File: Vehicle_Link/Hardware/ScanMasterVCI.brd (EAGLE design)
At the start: 53 x 39.4 mm, 97 parts, among them IC1 XMEGA32A4U, IC2 TL331, IC3 TL331, Q1 MMBT4403, Q10 ZXMP6A17G, Q2 MMBT3904, Q3 MMBT3904, Q4 MMBT4403, Q7 MMBT3904, Q8 MMBT4403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

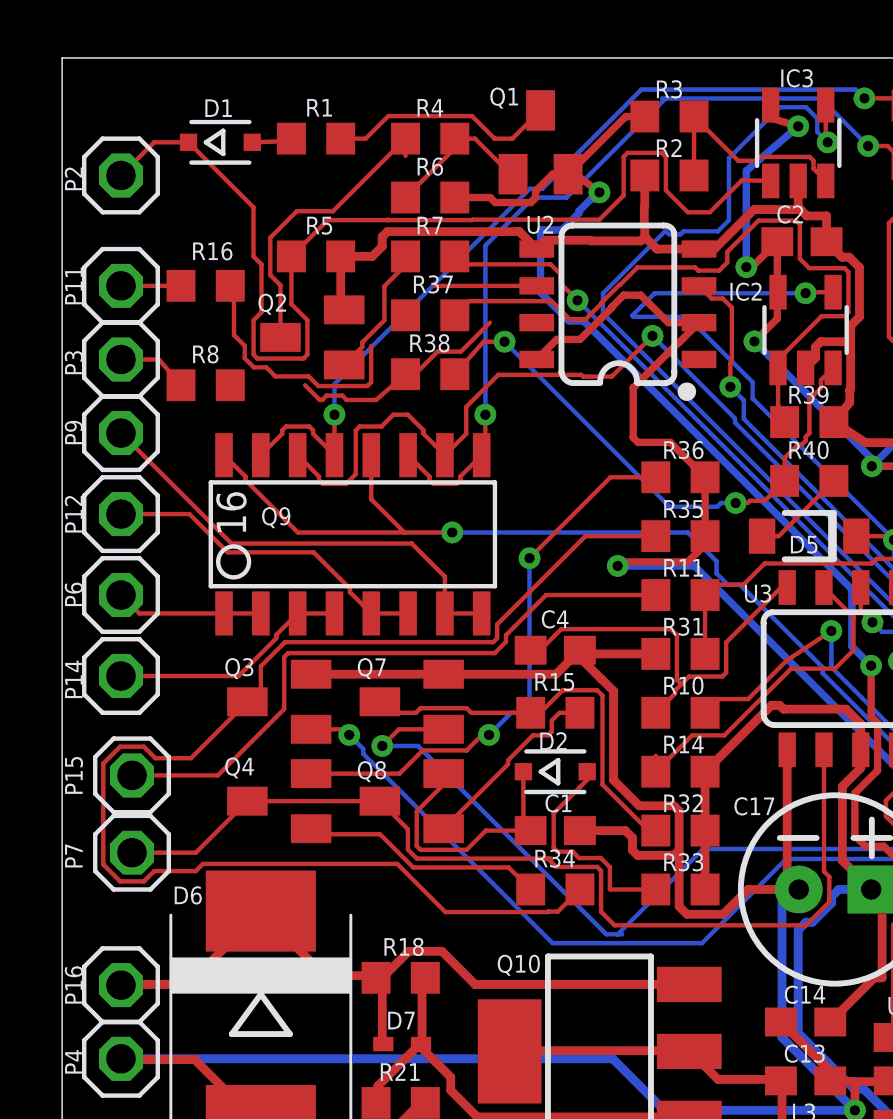
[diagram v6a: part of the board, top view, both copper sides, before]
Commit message: Some more minor changes to the schematic, some pull-up resistors needed to be moved for proper transistor-enabled pull-up resistor action. Tested on circuit, working OK now.
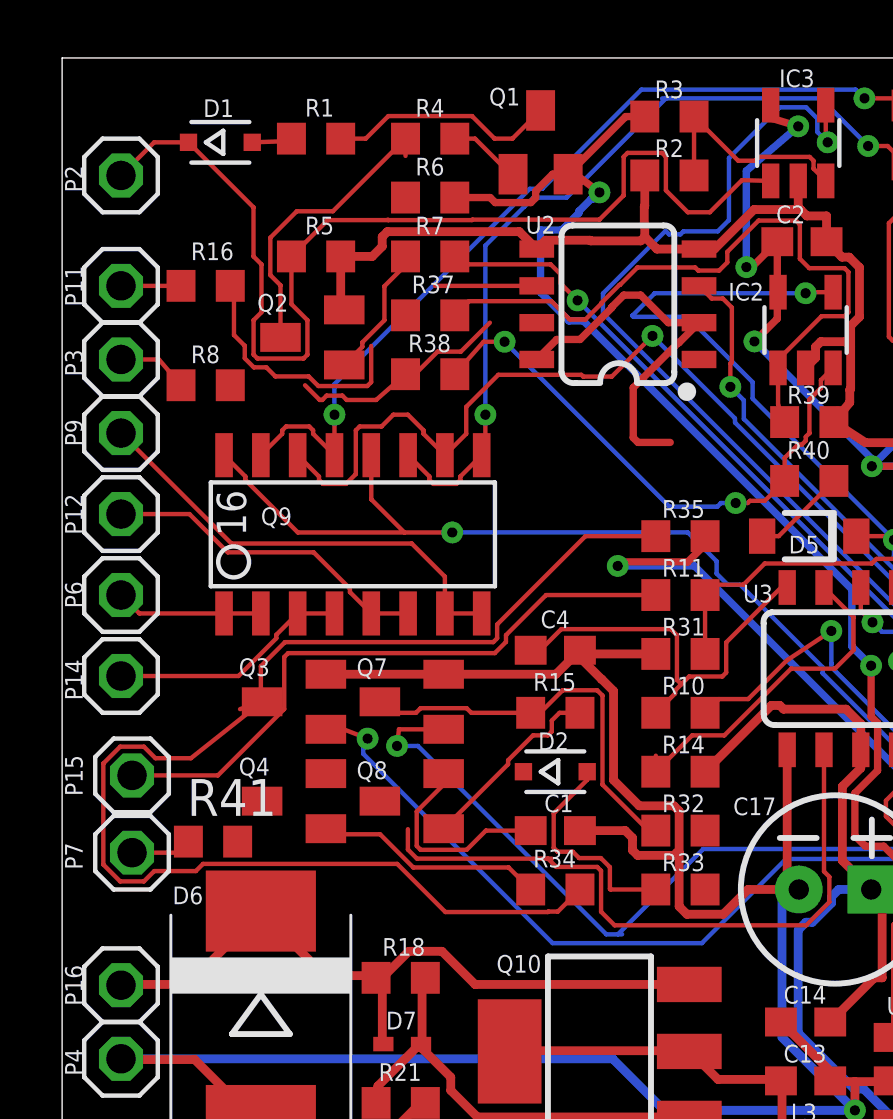
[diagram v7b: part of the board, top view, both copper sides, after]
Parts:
- removed R36: 1k, adafruit:R0603
- added R41: 1k, adafruit:R0603
- moved Q3 0.51 mm to (8.00, 17.1)
- moved Q4 0.51 mm to (8.00, 13.7)
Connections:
- removed net N$21: C1.1, D2.C, Q8.E
- new net N$32: Q8.C, R33.1
- net +12V: now also C1.1, Q8.E; no longer R33.1
- net +5V: now also Q4.E; no longer R36.2
- net J1962-7: now also D2.C, R41.1; no longer Q4.C, Q8.C
- net N$26: now also R6.1
- net N$28: no longer R6.1
- net N$31: now also Q4.C, R41.2; no longer Q4.E, R36.1
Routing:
- net N$31: track 19.3 -> 0.00 mm, vias 2 -> 0
- net N$21: track 9.33 -> 0.00 mm
- net J1962-7: track 33.7 -> 25.2 mm
- net +5V: track 82.5 -> 78.7 mm
- net +12V: track 68.4 -> 71.8 mm
- net N$28: track 5.35 -> 2.89 mm
- net N$13: track 27.4 -> 26.7 mm
- net N$23: track 45.2 -> 45.8 mm
- net GND: track 281.2 -> 280.7 mm

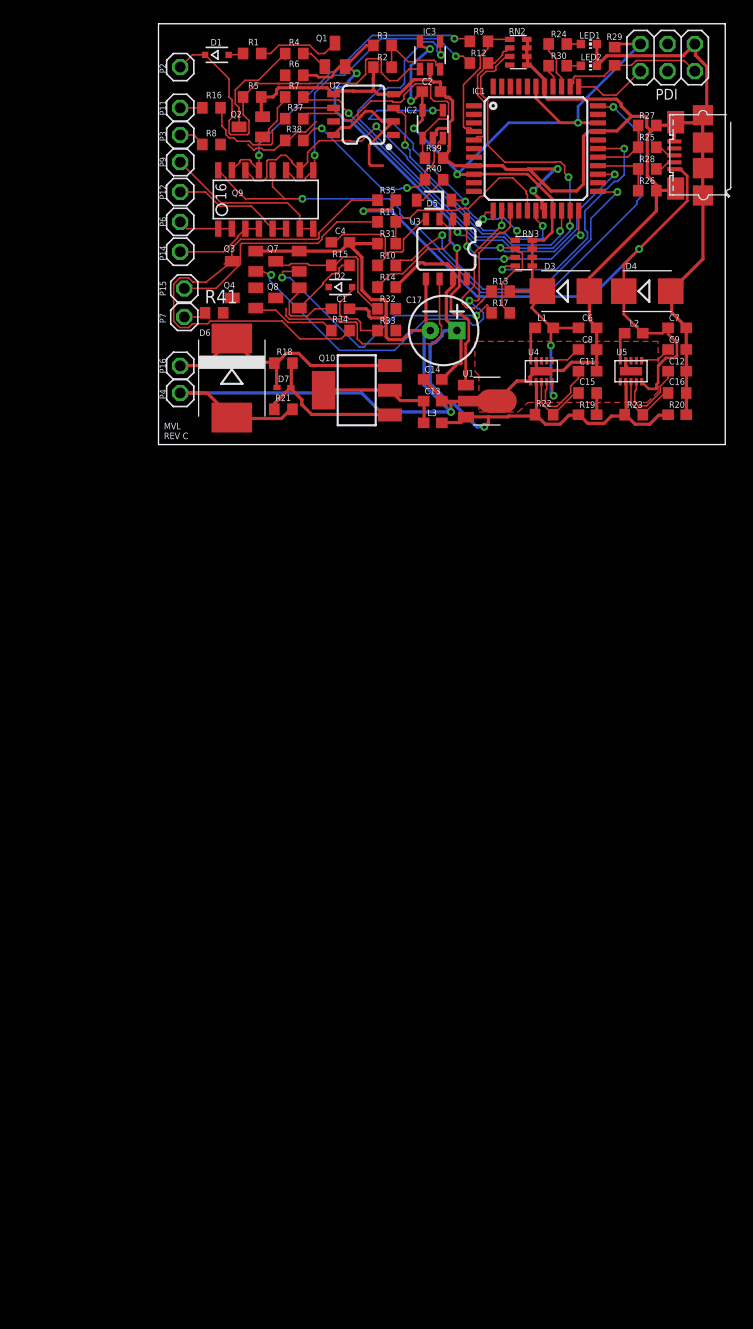
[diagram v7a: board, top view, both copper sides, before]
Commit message: Started experimenting with MOSFETs, added new parts to the library for the connector I'm planning on using.
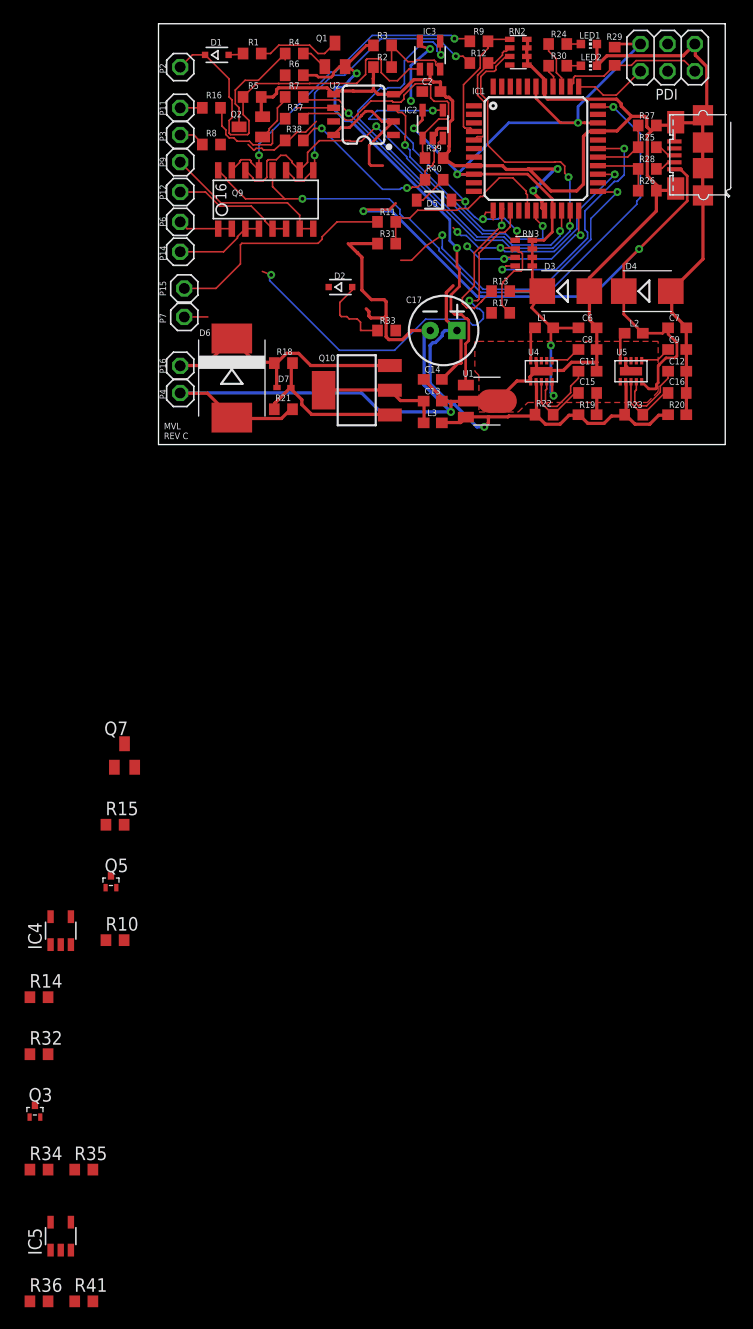
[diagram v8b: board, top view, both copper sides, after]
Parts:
- removed C1, C4: 220pF, adafruit:C0603
- removed Q4, Q8: MMBT4403, transistor-pnp:SOT23-BEC
- removed U3: SN65HVDA195-Q1, customics:SO08
- added IC4, IC5: TL331, linear:DBV-R-PDSO-G5
- added Q5: RUM002N05, customics:EMT3
- added R36: 1k, adafruit:R0603
- Q3: value MMBT3904 -> RUM002N05; device semicon-smd-ipc:SOT23 -> customics:EMT3
- R17, R34: value 1k -> 470
- R33: value 1k -> 10k
- moved R35 95.0 mm to (-6.99, -67.8)
- moved R41 93.3 mm to (-6.99, -80.1)
- moved R34 83.4 mm to (-11.2, -67.8), turned to 0 degrees
- moved Q3 81.9 mm to (-11.6, -62.4), turned to 0 degrees
- moved R32 76.9 mm to (-11.2, -57.0), turned to 0 degrees
- moved R14 74.0 mm to (-11.2, -51.7), turned to 0 degrees
- moved R10 68.0 mm to (-4.06, -46.4), turned to 0 degrees
- moved R15 56.4 mm to (-4.06, -35.6)
- moved Q7 48.7 mm to (-3.17, -29.1), turned to 0 degrees
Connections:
- removed net N$22: Q4.B, R34.2
- removed net N$23: Q3.3, R34.1, R35.1
- removed net N$31: Q4.C, R41.2
- removed net N$32: Q8.C, R33.1
- new net ISO-K: D2.C, IC4.1, Q5.2, Q7.3
- new net SCI-A-RX: IC5.1, Q3.2
- net +12V: now also IC4.5, IC5.5, R14.2, R33.1; no longer C1.1, Q8.E, R14.1, R32.1, U3.7
- net +3V3: now also R10.1, R35.1; no longer C2.1, IC2.5
- net +5V: now also C2.1, IC2.5, R36.2; no longer Q4.E, R35.2
- net GND: now also IC4.2, IC5.2, R32.1, R41.1; no longer C1.2, C4.2, Q3.2, U3.5
- net ISO-K-EN: no longer U3.2
- net ISO-K-RX: now also IC4.4; no longer U3.1
- net ISO-K-TX: now also R15.2; no longer R10.1
- net J1962-7: now also Q3.3, Q5.3; no longer D2.C, R41.1, U3.6
- net N$10: now also Q3.1, R34.1, R35.2; no longer C4.1, R10.2, U3.4
- net N$13: now also R15.1; no longer R17.1
- net N$14: now also IC5.3, R36.1, R41.2; no longer R14.2, U3.3
- net N$4: now also Q5.1, R10.2, R17.1; no longer Q7.3, R15.1, R32.2
- net N$8: now also IC4.3, R14.1, R32.2; no longer Q8.B, R15.2
- net SCI-A-RX-EN: now also R34.2; no longer Q3.1
- net SCI-ENGINE-RX: now also IC5.4
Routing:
- net N$23: track 45.8 -> 0.00 mm
- net N$13: track 26.7 -> 0.00 mm, vias 2 -> 0
- net J1962-7: track 25.2 -> 2.20 mm
- net +12V: track 71.8 -> 56.1 mm
- net GND: track 280.7 -> 265.1 mm
- net N$10: track 14.2 -> 0.00 mm
- net N$4: track 13.7 -> 0.00 mm
- net N$14: track 11.7 -> 0.00 mm
- net N$22: track 8.54 -> 0.00 mm
- net N$8: track 6.66 -> 0.00 mm
- net +3V3: track 93.3 -> 90.3 mm
- net ISO-K-RX: track 18.5 -> 15.6 mm
- net ISO-K-EN: track 32.1 -> 31.3 mm
- net ISO-K-TX: track 32.4 -> 31.7 mm
- net SCI-A-RX-EN: track 39.5 -> 38.9 mm
